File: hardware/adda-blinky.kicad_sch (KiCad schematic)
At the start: 35 parts, among them J1 AIN, J2 AOUT, J3 PB5, J4 COMM, J5 PWR, U2 ATtiny1616-M

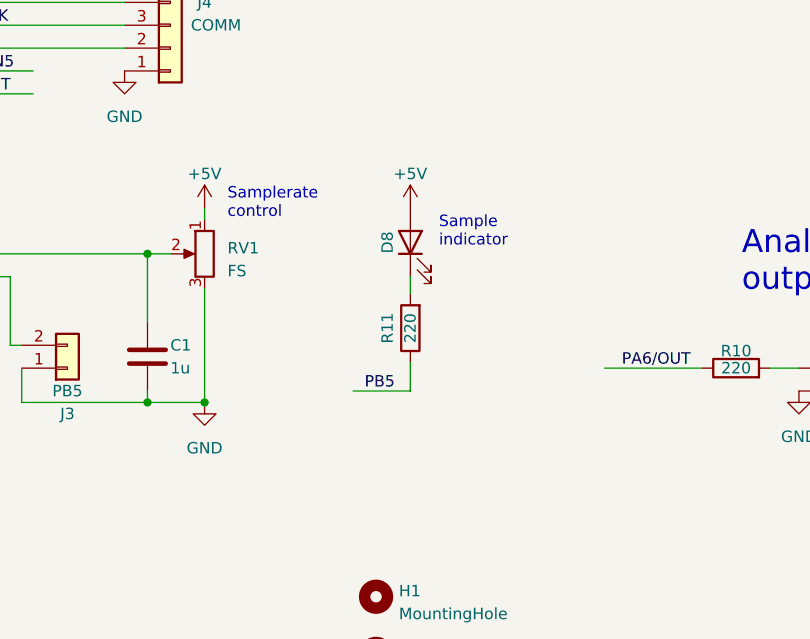
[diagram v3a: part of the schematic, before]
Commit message: Swap LED orientation
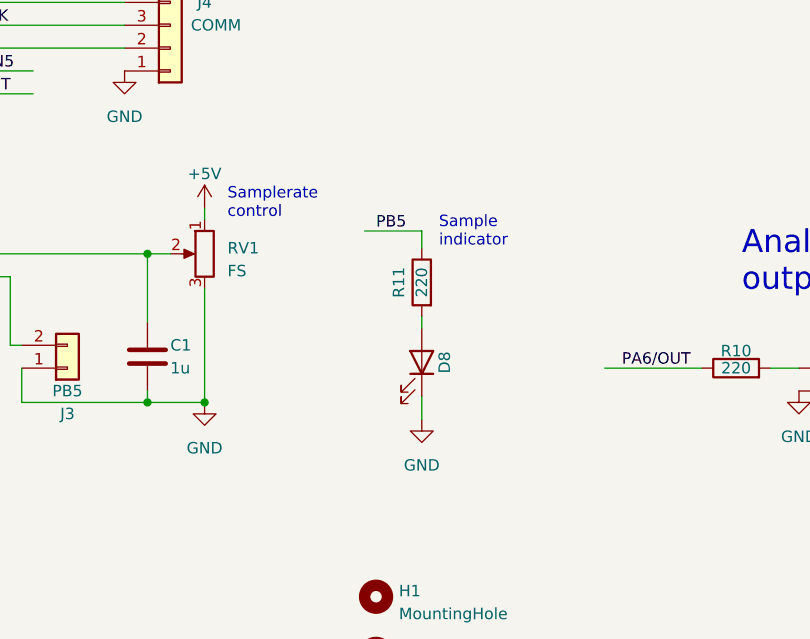
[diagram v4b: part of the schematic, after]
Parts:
- H2, H3, H4: footprint (none) -> MountingHole:MountingHole_3.2mm_M3_Pad
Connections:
- net +5V: no longer D8.2 (A)
- net GND: now also D8.1 (K)
- net at R11.2: now also D8.2 (A); no longer D8.1 (K)
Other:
- moved on the sheet: D8, R11
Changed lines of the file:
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@@
     (stroke (width 0) (type default))
   )
-  (wire (pts (xy 187.96 91.44) (xy 194.31 91.44))
+  (wire (pts (xy 189.23 73.66) (xy 195.58 73.66))
     (stroke (width 0) (type default))
   )
@@
     (stroke (width 0) (type default))
   )
+  (wire (pts (xy 195.58 94.615) (xy 195.58 92.075))
+    (stroke (width 0) (type default))
+  )
   (wire (pts (xy 140.97 48.26) (xy 162.56 48.26))
     (stroke (width 0) (type default))
@@
     (stroke (width 0) (type default))
   )
-  (wire (pts (xy 194.31 88.265) (xy 194.31 91.44))
+  (wire (pts (xy 195.58 75.565) (xy 195.58 73.66))
     (stroke (width 0) (type default))
   )
@@
     (stroke (width 0) (type default))
   )
-  (wire (pts (xy 194.31 80.645) (xy 194.31 78.74))
+  (wire (pts (xy 195.58 83.185) (xy 195.58 84.455))
     (stroke (width 0) (type default))
   )
@@
     (effects (font (size 1.27 1.27)) (justify left bottom))
   )
-  (label "PB5" (at 189.23 91.44 0) (fields_autoplaced)
+  (label "PB5" (at 190.5 73.66 0) (fields_autoplaced)
     (effects (font (size 1.27 1.27)) (justify left bottom))
   )
@@
     )
   )
-  (symbol (lib_id "power:+5V") (at 194.31 71.12 0) (unit 1)
-    (in_bom yes) (on_board yes) (dnp no) (fields_autoplaced)
-    (property "Reference" "#PWR02" (at 194.31 74.93 0)
-      (effects (font (size 1.27 1.27)) hide)
-    )
-    (property "Value" "+5V" (at 194.31 67.31 0)
-      (effects (font (size 1.27 1.27)))
-    )
-    (property "Footprint" "" (at 194.31 71.12 0)
-      (effects (font (size 1.27 1.27)) hide)
-    )
-    (property "Datasheet" "" (at 194.31 71.12 0)
-      (effects (font (size 1.27 1.27)) hide)
-    )
-    (pin "1")
-    (instances
-      (project "adda-blinky"
-        (path "/aa8d4fa8-9a28-4180-b4ba-75e5c4d6859f"
-          (reference "#PWR02") (unit 1)
-        )
-      )
-    )
-  )
   (symbol (lib_id "Device:R_Potentiometer") (at 171.45 76.2 0) (mirror y) (unit 1)
     (in_bom yes) (on_board yes) (dnp no) (fields_autoplaced)
@@
     )
   )
-  (symbol (lib_id "Device:LED") (at 194.31 74.93 90) (unit 1)
-    (in_bom yes) (on_board yes) (dnp no)
-    (property "Reference" "D8" (at 191.77 74.93 0)
-      (effects (font (size 1.27 1.27)))
-    )
-    (property "Value" "LED" (at 191.77 76.5175 0)
-      (effects (font (size 1.27 1.27)) hide)
-    )
-    (property "Footprint" "Diode_SMD:D_0805_2012Metric" (at 194.31 74.93 0)
-      (effects (font (size 1.27 1.27)) hide)
-    )
-    (property "Datasheet" "~" (at 194.31 74.93 0)
+  (symbol (lib_id "Device:LED") (at 195.58 88.265 270) (mirror x) (unit 1)
+    (in_bom yes) (on_board yes) (dnp no)
+    (property "Reference" "D8" (at 198.12 88.265 0)
+      (effects (font (size 1.27 1.27)))
+    )
+    (property "Value" "LED" (at 198.12 89.8525 0)
+      (effects (font (size 1.27 1.27)) hide)
+    )
+    (property "Footprint" "Diode_SMD:D_0805_2012Metric" (at 195.58 88.265 0)
+      (effects (font (size 1.27 1.27)) hide)
+    )
+    (property "Datasheet" "~" (at 195.58 88.265 0)
       (effects (font (size 1.27 1.27)) hide)
     )
@@
       (effects (font (size 1.27 1.27)) (justify left))
     )
-    (property "Footprint" "" (at 190.5 134.62 0)
+    (property "Footprint" "MountingHole:MountingHole_3.2mm_M3_Pad" (at 190.5 134.62 0)
       (effects (font (size 1.27 1.27)) hide)
     )
@@
       (effects (font (size 1.27 1.27)) (justify left))
     )
-    (property "Footprint" "" (at 190.5 128.27 0)
+    (property "Footprint" "MountingHole:MountingHole_3.2mm_M3_Pad" (at 190.5 128.27 0)
       (effects (font (size 1.27 1.27)) hide)
     )
@@
         (path "/aa8d4fa8-9a28-4180-b4ba-75e5c4d6859f"
           (reference "#PWR015") (unit 1)
+        )
+      )
+    )
+  )
+  (symbol (lib_id "power:GND") (at 195.58 94.615 0) (unit 1)
+    (in_bom yes) (on_board yes) (dnp no) (fields_autoplaced)
+    (property "Reference" "#PWR02" (at 195.58 100.965 0)
+      (effects (font (size 1.27 1.27)) hide)
+    )
+    (property "Value" "GND" (at 195.58 99.695 0)
+      (effects (font (size 1.27 1.27)))
+    )
+    (property "Footprint" "" (at 195.58 94.615 0)
+      (effects (font (size 1.27 1.27)) hide)
+    )
+    (property "Datasheet" "" (at 195.58 94.615 0)
+      (effects (font (size 1.27 1.27)) hide)
+    )
+    (pin "1")
+    (instances
+      (project "adda-blinky"
+        (path "/aa8d4fa8-9a28-4180-b4ba-75e5c4d6859f"
+          (reference "#PWR02") (unit 1)
         )
       )
@@
     )
   )
-  (symbol (lib_id "Device:R") (at 194.31 84.455 180) (unit 1)
-    (in_bom yes) (on_board yes) (dnp no)
-    (property "Reference" "R11" (at 191.77 84.455 90)
-      (effects (font (size 1.27 1.27)))
-    )
-    (property "Value" "220" (at 194.31 84.455 90)
-      (effects (font (size 1.27 1.27)))
-    )
-    (property "Footprint" "Resistor_SMD:R_0805_2012Metric" (at 196.088 84.455 90)
-      (effects (font (size 1.27 1.27)) hide)
-    )
-    (property "Datasheet" "~" (at 194.31 84.455 0)
+  (symbol (lib_id "Device:R") (at 195.58 79.375 0) (mirror y) (unit 1)
+    (in_bom yes) (on_board yes) (dnp no)
+    (property "Reference" "R11" (at 193.04 79.375 90)
+      (effects (font (size 1.27 1.27)))
+    )
+    (property "Value" "220" (at 195.58 79.375 90)
+      (effects (font (size 1.27 1.27)))
+    )
+    (property "Footprint" "Resistor_SMD:R_0805_2012Metric" (at 197.358 79.375 90)
+      (effects (font (size 1.27 1.27)) hide)
+    )
+    (property "Datasheet" "~" (at 195.58 79.375 0)
       (effects (font (size 1.27 1.27)) hide)
     )
@@
       (effects (font (size 1.27 1.27)) (justify left))
     )
-    (property "Footprint" "" (at 190.5 120.65 0)
-      (effects (font (size 1.27 1.27)) hide)
-    )
+    (property "Footprint" "MountingHole:MountingHole_3.2mm_M3_Pad" (at 190.5 120.65 0)
+      (effects (font (size 1.27 1.27)) hide)
+    )
